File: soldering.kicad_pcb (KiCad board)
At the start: 2 copper layers, 50.8 x 50.8 mm, 41 parts, among them CON1 BARREL_JACK, IC1 AT90PWM1-S, IC2 ATTINY10-P, IC3 ATTINY10-P, IC4 AT89S2051-S, U1 LM7905CT

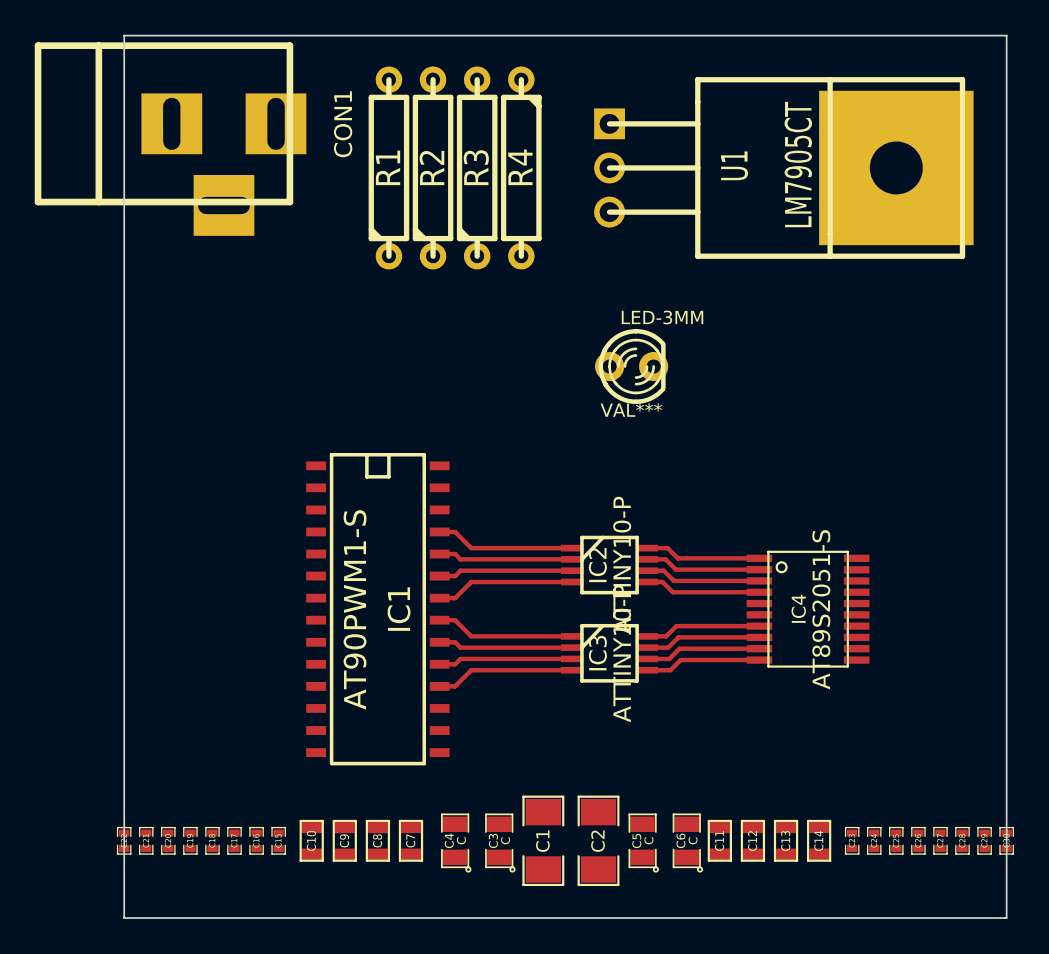
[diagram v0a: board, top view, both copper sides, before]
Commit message: Added an LED, via, and Logo
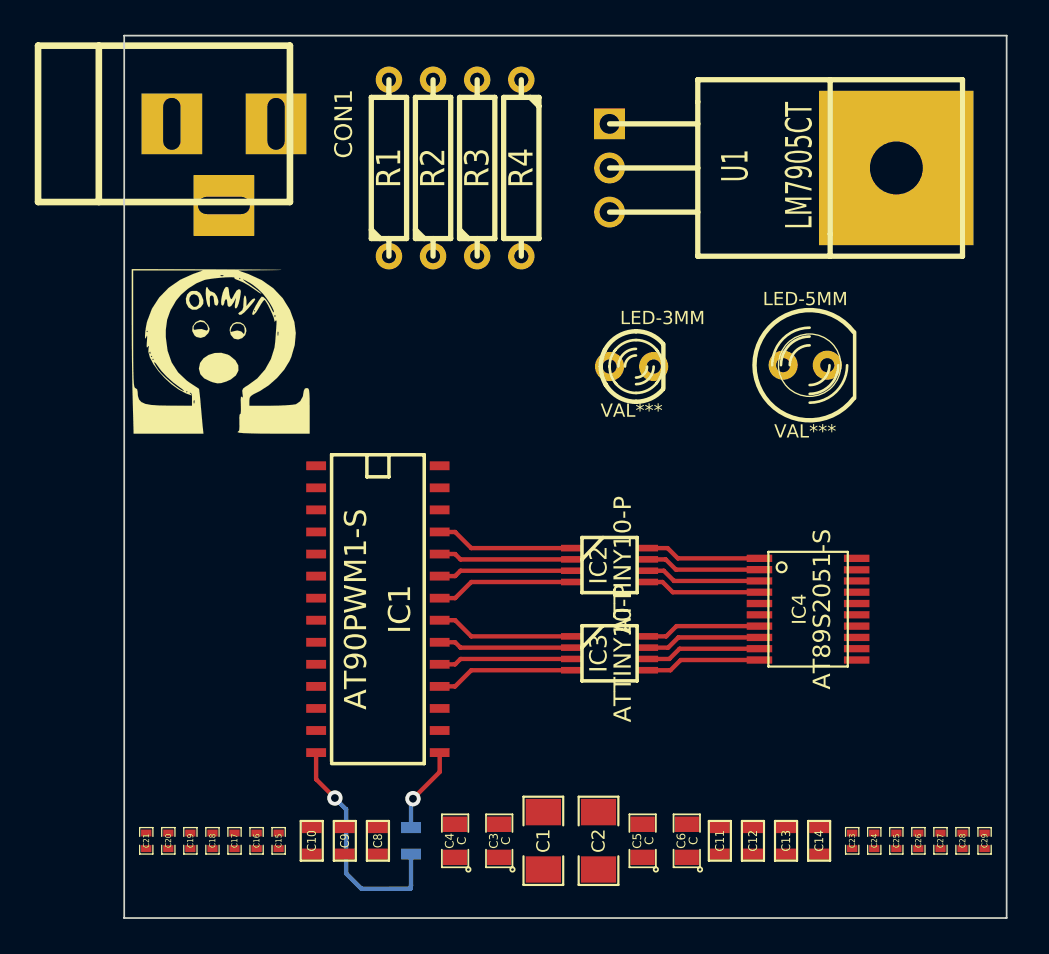
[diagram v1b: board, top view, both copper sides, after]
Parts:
- removed C22, C30: C, SM0402
- added ?: , LOGO, F.Cu at (183.3, 109.6)
- added LED-5MM: VAL***, LED-5MM, F.Cu at (217.0, 110.4)
- C7: moved to B.Cu
- turned C7 to 270 degrees
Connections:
- C7 pad 1: (no net) -> N-0000051
- C7 pad 2: (no net) -> N-0000050
- IC1 pad 14: (no net) -> N-0000050
- IC1 pad 15: (no net) -> N-0000051
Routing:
- net N-0000050: track 0.00 -> 13.7 mm, vias 0 -> 1
- net N-0000051: track 0.00 -> 5.00 mm, vias 0 -> 1
